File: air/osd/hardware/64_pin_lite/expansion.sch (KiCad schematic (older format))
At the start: 6 parts, among them P11 CONN_1, P2 CONN_20, P3 CONN_20

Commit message: removed vin+ for bat and added pin. Looks nearly done now
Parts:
- added P13: CONN_1, symbol CONN_1
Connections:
- net VIN+: no longer R30.1
- new net: P13.1, R30.1
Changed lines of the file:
@@
-EESchema Schematic File Version 2  date Sun 08 Mar 2015 12:24:24 GMT
+EESchema Schematic File Version 2  date Mon 09 Mar 2015 16:29:56 GMT
 LIBS:lm358
 LIBS:conn_6
@@
 Sheet 5 8
 Title ""
-Date "8 mar 2015"
+Date "9 mar 2015"
 Rev ""
 Comp ""
@@
 Comment4 ""
 $EndDescr
+$Comp
+L CONN_1 P13
+U 1 1 54FDC7F4
+P 5600 2900
+F 0 "P13" H 5680 2900 40  0000 L CNN
+F 1 "CONN_1" H 5600 2955 30  0001 C CNN
+	1    5600 2900
+	1    0    0    -1
+$EndComp
 Wire Wire Line
 	6600 3400 6500 3400
@@
 	6500 4400 6600 4400
 Wire Wire Line
-	5100 2850 5300 2850
-Wire Wire Line
-	5300 2850 5300 3050
+	5450 2900 5300 2900
+Wire Wire Line
+	5300 2900 5300 3050
 Wire Wire Line
 	5300 3650 5550 3650
@@
 	1    0    0    -1
 $EndComp
-Text HLabel 5100 2850 0    45   Input ~ 0
-VIN+
 Text HLabel 5200 4300 0    45   BiDi ~ 0
 MCU_GND

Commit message: hopefully finished
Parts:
- removed C39: 10uF, symbol C
- removed P13: CONN_1, symbol CONN_1
- removed R30: 110K, symbol R
- removed R31: 15K, symbol R
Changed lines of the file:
@@
-EESchema Schematic File Version 2  date Wed 11 Mar 2015 10:11:51 GMT
+EESchema Schematic File Version 2  date Wed 11 Mar 2015 17:51:25 GMT
 LIBS:lm358
 LIBS:conn_6
@@
 Comment4 ""
 $EndDescr
-$Comp
-L CONN_1 P13
-U 1 1 54FDC7F4
-P 5600 2900
-F 0 "P13" H 5680 2900 40  0000 L CNN
-F 1 "CONN_1" H 5600 2955 30  0001 C CNN
-	1    5600 2900
-	1    0    0    -1
-$EndComp
+Text HLabel 4200 3000 2    45   BiDi ~ 0
+XP_PB1
 Wire Wire Line
 	6600 3400 6500 3400
@@
 Wire Wire Line
 	6600 1750 6600 1800
-Connection ~ 5300 4300
-Wire Wire Line
-	5550 4200 5550 4300
-Wire Wire Line
-	5550 4300 5200 4300
-Wire Wire Line
-	5300 4200 5300 4300
-Wire Wire Line
-	5300 3550 5300 3700
 Wire Wire Line
 	6500 4300 6600 4300
@@
 	4100 3200 4200 3200
 Wire Wire Line
-	4750 3000 4100 3000
+	4200 3000 4100 3000
 Connection ~ 6200 2500
 Wire Wire Line
@@
 Wire Wire Line
 	6500 4400 6600 4400
-Wire Wire Line
-	5450 2900 5300 2900
-Wire Wire Line
-	5300 2900 5300 3050
-Wire Wire Line
-	5300 3650 5550 3650
-Wire Wire Line
-	5550 3650 5550 3800
-Connection ~ 5300 3650
-Wire Wire Line
-	5300 3600 4650 3600
-Connection ~ 5300 3600
-Wire Wire Line
-	4650 3600 4650 3000
-Connection ~ 4650 3000
 Wire Wire Line
 	4100 3400 4200 3400
@@
 Text Notes 5500 3350 0    45   ~ 0
 3V max. \nWith values \nshown works \nfrom 2S to 6S\n
-$Comp
-L C C39
-U 1 1 547ED333
-P 5550 4000
-F 0 "C39" H 5600 4100 50  0000 L CNN
-F 1 "10uF" H 5600 3900 50  0000 L CNN
-	1    5550 4000
-	1    0    0    -1
-$EndComp
-Text HLabel 5200 4300 0    45   BiDi ~ 0
-MCU_GND
-$Comp
-L R R31
-U 1 1 547ED2AB
-P 5300 3950
-F 0 "R31" V 5380 3950 50  0000 C CNN
-F 1 "15K" V 5300 3950 50  0000 C CNN
-	1    5300 3950
-	1    0    0    -1
-$EndComp
-$Comp
-L R R30
-U 1 1 547ED2A5
-P 5300 3300
-F 0 "R30" V 5380 3300 50  0000 C CNN
-F 1 "110K" V 5300 3300 50  0000 C CNN
-	1    5300 3300
-	1    0    0    -1
-$EndComp
 Text HLabel 6500 4400 0    45   BiDi ~ 0
 XP_GND
@@
 XP_GND
 $Comp
-L PWR_FLAG #FLG3
+L PWR_FLAG #FLG03
 U 1 1 5474845E
 P 5550 2550
-F 0 "#FLG3" H 5550 2820 30  0001 C CNN
+F 0 "#FLG03" H 5550 2820 30  0001 C CNN
 F 1 "PWR_FLAG" H 5550 2780 30  0000 C CNN
 	1    5550 2550
@@
 $EndComp
 $Comp
-L PWR_FLAG #FLG4
+L PWR_FLAG #FLG04
 U 1 1 54748449
 P 6200 2350
-F 0 "#FLG4" H 6200 2620 30  0001 C CNN
+F 0 "#FLG04" H 6200 2620 30  0001 C CNN
 F 1 "PWR_FLAG" H 6200 2580 30  0000 C CNN
 	1    6200 2350
@@
 Text HLabel 4200 4400 2    45   BiDi ~ 0
 XP_GND
-Text HLabel 4750 3000 2    45   BiDi ~ 0
-XP_PB1
 $EndSCHEMATC

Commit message: after sending V2 board to OSHPark, v2.1
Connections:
- net XP_+3V: now also P2.16 (P16); no longer P2.15 (P15)
- net XP_GND: now also P2.12 (P12), P2.18 (P18), P2.2 (P2), P2.5 (P5), P2.8 (P8), P3.14 (P14); no longer P2.17 (P17), P2.20 (P20), P2.3 (P3), P2.4 (P4), P3.10 (P10)
- net XP_NRST: now also P2.20 (P20); no longer P2.19 (P19)
- net XP_PA0: now also P3.13 (P13); no longer P3.14 (P14)
- net XP_PA1: now also P3.12 (P12); no longer P3.13 (P13)
- net XP_PA11: now also P2.14 (P14); no longer P2.13 (P13)
- net XP_PA12: now also P2.15 (P15); no longer P2.14 (P14)
- net XP_PA13: now also P2.19 (P19); no longer P2.18 (P18)
- net XP_PA14: now also P2.17 (P17); no longer P2.16 (P16)
- net XP_PB6: now also P2.7 (P7); no longer P2.8 (P8)
- net XP_PB7: now also P2.6 (P6); no longer P2.7 (P7)
- net XP_PB8: now also P2.4 (P4); no longer P2.6 (P6)
- net XP_PB9: now also P2.3 (P3); no longer P2.5 (P5)
- net XP_PC0: now also P3.10 (P10); no longer P3.11 (P11)
- net XP_PC1: now also P3.11 (P11); no longer P3.12 (P12)
- net XP_PC12: now also P2.13 (P13); no longer P2.12 (P12)
- no-connect marks 1 -> 0
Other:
- note removed: "3V max. \nWith values \nshown works \nfrom 2S to 6S\n"
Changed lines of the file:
@@
-EESchema Schematic File Version 2  date Wed 11 Mar 2015 17:51:25 GMT
+EESchema Schematic File Version 2  date Thu 12 Mar 2015 15:44:15 GMT
 LIBS:lm358
 LIBS:conn_6
@@
 Sheet 5 8
 Title ""
-Date "11 mar 2015"
+Date "12 mar 2015"
 Rev ""
 Comp ""
@@
 Comment4 ""
 $EndDescr
+Wire Wire Line
+	6600 2700 6500 2700
+Wire Wire Line
+	6600 3400 6500 3400
+Wire Wire Line
+	6600 3200 6500 3200
+Wire Wire Line
+	6600 3000 6500 3000
+Wire Wire Line
+	6500 1750 6600 1750
+Wire Wire Line
+	6600 1750 6600 1800
+Wire Wire Line
+	6500 4300 6600 4300
+Wire Wire Line
+	6500 4100 6600 4100
+Wire Wire Line
+	6500 3900 6600 3900
+Wire Wire Line
+	6500 3700 6600 3700
+Wire Wire Line
+	6500 3500 6600 3500
+Wire Wire Line
+	6500 2900 6600 2900
+Wire Wire Line
+	4100 4400 4200 4400
+Wire Wire Line
+	4100 4200 4200 4200
+Wire Wire Line
+	4100 4000 4200 4000
+Wire Wire Line
+	4100 3800 4200 3800
+Wire Wire Line
+	4100 3600 4200 3600
+Wire Wire Line
+	4100 3200 4200 3200
+Wire Wire Line
+	4200 3000 4100 3000
+Connection ~ 6200 2500
+Wire Wire Line
+	6200 2350 6200 2500
+Wire Wire Line
+	4100 2700 4200 2700
+Wire Wire Line
+	4100 2500 4200 2500
+Wire Wire Line
+	4100 2900 4200 2900
+Wire Wire Line
+	5950 2500 6600 2500
+Wire Wire Line
+	4100 2600 4200 2600
+Wire Wire Line
+	4100 2800 4200 2800
+Wire Wire Line
+	5550 2700 5550 2550
+Connection ~ 5550 2700
+Wire Wire Line
+	4100 3100 4200 3100
+Wire Wire Line
+	4100 3300 4200 3300
+Wire Wire Line
+	4100 3500 4200 3500
+Wire Wire Line
+	4100 3700 4200 3700
+Wire Wire Line
+	4100 3900 4200 3900
+Wire Wire Line
+	4100 4100 4200 4100
+Wire Wire Line
+	4100 4300 4200 4300
+Wire Wire Line
+	6500 2800 6600 2800
+Wire Wire Line
+	6500 3600 6600 3600
+Wire Wire Line
+	6500 3800 6600 3800
+Wire Wire Line
+	6500 4000 6600 4000
+Wire Wire Line
+	6500 4200 6600 4200
+Wire Wire Line
+	6500 4400 6600 4400
+Wire Wire Line
+	4100 3400 4200 3400
+Wire Wire Line
+	6600 3100 6500 3100
+Wire Wire Line
+	6600 3300 6500 3300
+Wire Wire Line
+	6600 2600 5650 2600
+Wire Wire Line
+	5650 2600 5650 2700
+Wire Wire Line
+	5650 2700 5400 2700
+Text HLabel 6500 2900 0    45   BiDi ~ 0
+XP_GND
 Text HLabel 4200 3000 2    45   BiDi ~ 0
 XP_PB1
-Wire Wire Line
-	6600 3400 6500 3400
-Wire Wire Line
-	6600 3200 6500 3200
-Wire Wire Line
-	6600 3000 6500 3000
-Wire Wire Line
-	6500 1750 6600 1750
-Wire Wire Line
-	6600 1750 6600 1800
-Wire Wire Line
-	6500 4300 6600 4300
-Wire Wire Line
-	6500 4100 6600 4100
-Wire Wire Line
-	6500 3900 6600 3900
-Wire Wire Line
-	6500 3700 6600 3700
-Wire Wire Line
-	6500 3500 6600 3500
-Wire Wire Line
-	6500 2900 6600 2900
-Wire Wire Line
-	4100 4400 4200 4400
-Wire Wire Line
-	4100 4200 4200 4200
-Wire Wire Line
-	4100 4000 4200 4000
-Wire Wire Line
-	4100 3800 4200 3800
-Wire Wire Line
-	4100 3600 4200 3600
-Wire Wire Line
-	4100 3200 4200 3200
-Wire Wire Line
-	4200 3000 4100 3000
-Connection ~ 6200 2500
-Wire Wire Line
-	6200 2350 6200 2500
-Wire Wire Line
-	4100 2700 4200 2700
-Wire Wire Line
-	4100 2500 4200 2500
-Wire Wire Line
-	4100 2900 4200 2900
-Wire Wire Line
-	5400 2700 6600 2700
-Wire Wire Line
-	6600 2500 5950 2500
-Wire Wire Line
-	4100 2600 4200 2600
-Wire Wire Line
-	4100 2800 4200 2800
-Wire Wire Line
-	5550 2550 5550 2700
-Connection ~ 5550 2700
-Wire Wire Line
-	4100 3100 4200 3100
-Wire Wire Line
-	4100 3300 4200 3300
-Wire Wire Line
-	4100 3500 4200 3500
-Wire Wire Line
-	4100 3700 4200 3700
-Wire Wire Line
-	4100 3900 4200 3900
-Wire Wire Line
-	4100 4100 4200 4100
-Wire Wire Line
-	4100 4300 4200 4300
-Wire Wire Line
-	6500 2800 6600 2800
-Wire Wire Line
-	6500 3600 6600 3600
-Wire Wire Line
-	6500 3800 6600 3800
-Wire Wire Line
-	6500 4000 6600 4000
-Wire Wire Line
-	6500 4200 6600 4200
-Wire Wire Line
-	6500 4400 6600 4400
-Wire Wire Line
-	4100 3400 4200 3400
-Wire Wire Line
-	6600 3100 6500 3100
-Wire Wire Line
-	6600 3300 6500 3300
-Text HLabel 6500 3000 0    45   BiDi ~ 0
+Text HLabel 6500 2800 0    45   BiDi ~ 0
 XP_PB8
-Text HLabel 4200 3400 2    45   BiDi ~ 0
-XP_GND
-NoConn ~ 6600 2600
+Text HLabel 4200 3800 2    45   BiDi ~ 0
+XP_GND
 Text HLabel 6500 1750 0    45   Output ~ 0
 VIN-
@@
 	0    1    1    0
 $EndComp
-Text Notes 5500 3350 0    45   ~ 0
-3V max. \nWith values \nshown works \nfrom 2S to 6S\n
-Text HLabel 6500 4400 0    45   BiDi ~ 0
-XP_GND
-Text HLabel 6500 2800 0    45   Output ~ 0
+Text HLabel 6500 3600 0    45   BiDi ~ 0
+XP_GND
+Text HLabel 6500 3200 0    45   Output ~ 0
 XP_GND
 $Comp
@@
 	1    0    0    -1
 $EndComp
-Text HLabel 6500 4200 0    45   BiDi ~ 0
+Text HLabel 6500 4300 0    45   BiDi ~ 0
 XP_PA13
 Text HLabel 4200 2800 2    45   Output ~ 0
@@
 Text HLabel 4200 3200 2    45   Input ~ 0
 XP_PC15
-Text HLabel 6500 4300 0    45   Output ~ 0
+Text HLabel 6500 4400 0    45   Output ~ 0
 XP_NRST
 Text HLabel 1900 5450 0    45   BiDi ~ 0
 XP_GND
+Text HLabel 6500 4200 0    45   BiDi ~ 0
+XP_GND
 Text HLabel 6500 4100 0    45   BiDi ~ 0
-XP_GND
-Text HLabel 6500 4000 0    45   BiDi ~ 0
 XP_PA14
+Text HLabel 6500 3900 0    45   BiDi ~ 0
+XP_PA12
 Text HLabel 6500 3800 0    45   BiDi ~ 0
-XP_PA12
+XP_PA11
 Text HLabel 6500 3700 0    45   BiDi ~ 0
-XP_PA11
-Text HLabel 6500 3600 0    45   BiDi ~ 0
 XP_PC12
 Text HLabel 6500 3500 0    45   BiDi ~ 0
@@
 Text HLabel 6500 3300 0    45   BiDi ~ 0
 XP_PB5
-Text HLabel 6500 3900 0    45   BiDi ~ 0
+Text HLabel 6500 4000 0    45   BiDi ~ 0
 XP_+3V
-Text HLabel 6500 3200 0    45   BiDi ~ 0
+Text HLabel 6500 3100 0    45   BiDi ~ 0
 XP_PB6
-Text HLabel 6500 3100 0    45   BiDi ~ 0
+Text HLabel 6500 3000 0    45   BiDi ~ 0
 XP_PB7
-Text HLabel 6500 2900 0    45   BiDi ~ 0
+Text HLabel 6500 2700 0    45   BiDi ~ 0
 XP_PB9
 Text HLabel 4200 4300 2    45   BiDi ~ 0
@@
 Text HLabel 4200 3900 2    45   BiDi ~ 0
 XP_PC3
-Text HLabel 4200 3800 2    45   BiDi ~ 0
+Text HLabel 4200 3700 2    45   BiDi ~ 0
 XP_PA0
-Text HLabel 4200 3700 2    45   BiDi ~ 0
+Text HLabel 4200 3600 2    45   BiDi ~ 0
 XP_PA1
-Text HLabel 4200 3600 2    45   BiDi ~ 0
+Text HLabel 4200 3500 2    45   BiDi ~ 0
 XP_PC1
-Text HLabel 4200 3500 2    45   BiDi ~ 0
+Text HLabel 4200 3400 2    45   BiDi ~ 0
 XP_PC0
 Text HLabel 4200 3300 2    45   BiDi ~ 0

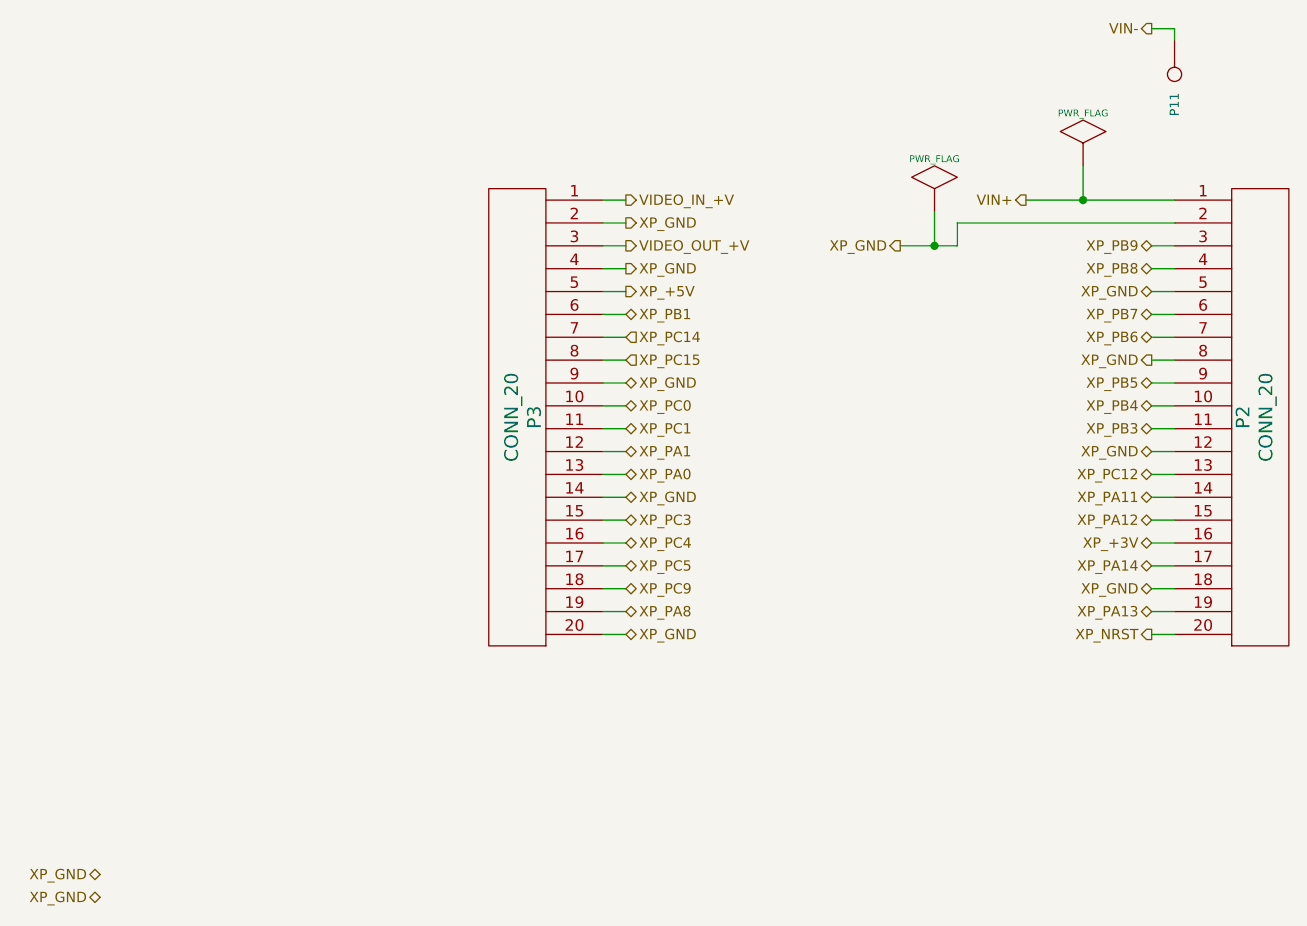
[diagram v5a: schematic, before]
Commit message: added some 3 terminal EMI filters to the board
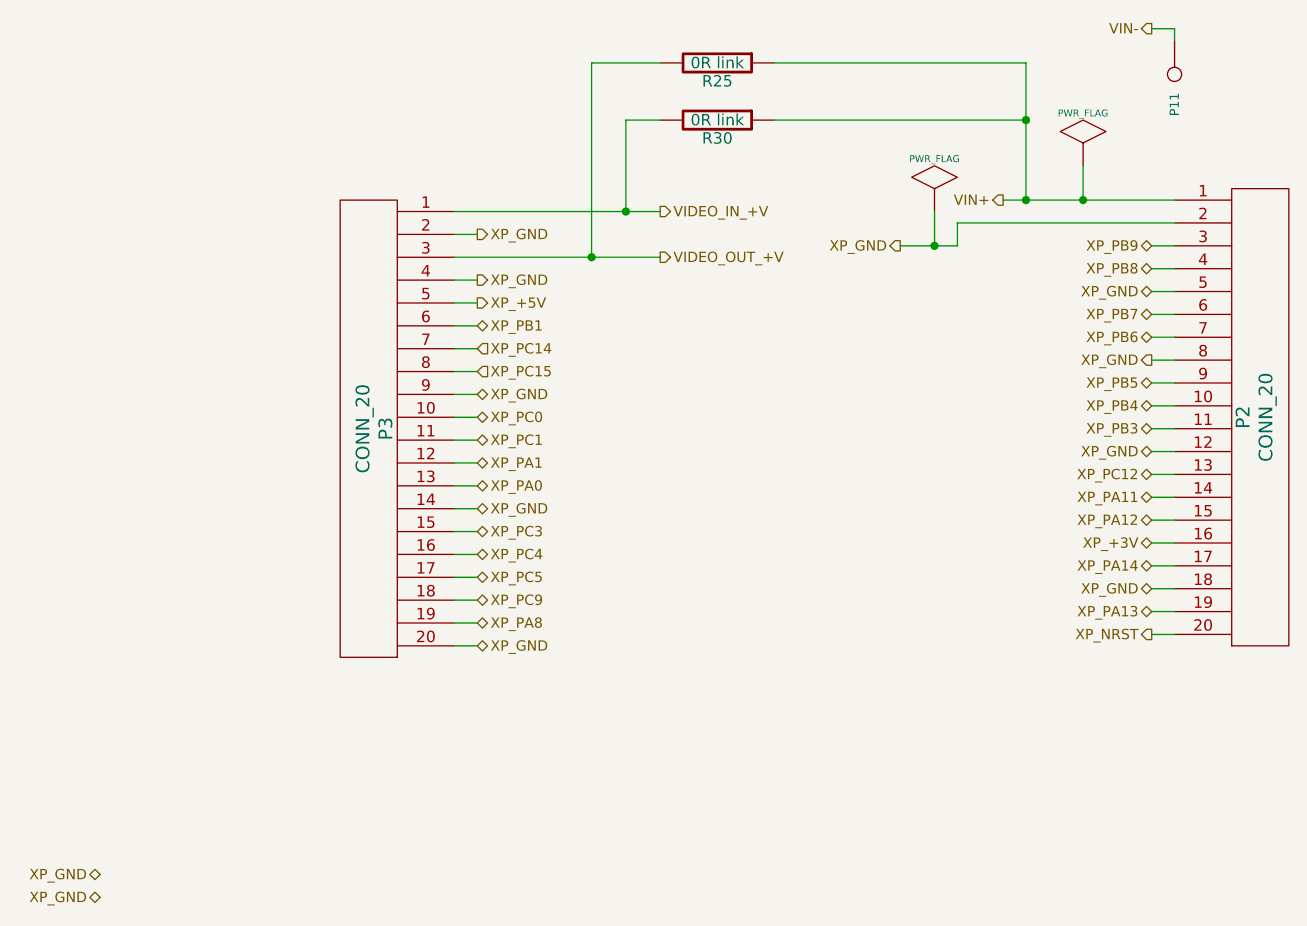
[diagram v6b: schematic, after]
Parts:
- added R25, R30: 0R link, symbol R
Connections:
- net VIDEO_IN_+V: now also R30.2
- net VIDEO_OUT_+V: now also R25.2
- net VIN+: now also R25.1, R30.1
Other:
- moved on the sheet: P3
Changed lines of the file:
@@
-EESchema Schematic File Version 2  date Thu 12 Mar 2015 15:44:15 GMT
+EESchema Schematic File Version 2  date Wed 17 Jun 2015 00:34:32 BST
 LIBS:lm358
 LIBS:conn_6
@@
 LIBS:74lvc1g86
 LIBS:R0link
+LIBS:emi_filter
 LIBS:osd-cache
 EELAYER 25  0
@@
 Sheet 5 8
 Title ""
-Date "12 mar 2015"
+Date "16 jun 2015"
 Rev ""
 Comp ""
@@
 Comment4 ""
 $EndDescr
+Connection ~ 4050 2750
+Wire Wire Line
+	4350 1900 4050 1900
+Wire Wire Line
+	4050 1900 4050 2750
+Connection ~ 5950 2150
+Wire Wire Line
+	4850 2150 5950 2150
 Wire Wire Line
 	6600 2700 6500 2700
@@
 	6500 2900 6600 2900
 Wire Wire Line
-	4100 4400 4200 4400
-Wire Wire Line
-	4100 4200 4200 4200
-Wire Wire Line
-	4100 4000 4200 4000
-Wire Wire Line
-	4100 3800 4200 3800
-Wire Wire Line
-	4100 3600 4200 3600
-Wire Wire Line
-	4100 3200 4200 3200
-Wire Wire Line
-	4200 3000 4100 3000
+	3450 4450 3550 4450
+Wire Wire Line
+	3450 4250 3550 4250
+Wire Wire Line
+	3450 4050 3550 4050
+Wire Wire Line
+	3450 3850 3550 3850
+Wire Wire Line
+	3450 3650 3550 3650
+Wire Wire Line
+	3450 3250 3550 3250
+Wire Wire Line
+	3550 3050 3450 3050
 Connection ~ 6200 2500
 Wire Wire Line
 	6200 2350 6200 2500
 Wire Wire Line
-	4100 2700 4200 2700
-Wire Wire Line
-	4100 2500 4200 2500
-Wire Wire Line
-	4100 2900 4200 2900
-Wire Wire Line
-	5950 2500 6600 2500
-Wire Wire Line
-	4100 2600 4200 2600
-Wire Wire Line
-	4100 2800 4200 2800
+	3450 2750 4350 2750
+Wire Wire Line
+	3450 2550 4350 2550
+Wire Wire Line
+	3450 2950 3550 2950
+Wire Wire Line
+	6600 2500 5850 2500
+Wire Wire Line
+	3450 2650 3550 2650
+Wire Wire Line
+	3450 2850 3550 2850
 Wire Wire Line
 	5550 2700 5550 2550
 Connection ~ 5550 2700
 Wire Wire Line
-	4100 3100 4200 3100
-Wire Wire Line
-	4100 3300 4200 3300
-Wire Wire Line
-	4100 3500 4200 3500
-Wire Wire Line
-	4100 3700 4200 3700
-Wire Wire Line
-	4100 3900 4200 3900
-Wire Wire Line
-	4100 4100 4200 4100
-Wire Wire Line
-	4100 4300 4200 4300
+	3450 3150 3550 3150
+Wire Wire Line
+	3450 3350 3550 3350
+Wire Wire Line
+	3450 3550 3550 3550
+Wire Wire Line
+	3450 3750 3550 3750
+Wire Wire Line
+	3450 3950 3550 3950
+Wire Wire Line
+	3450 4150 3550 4150
+Wire Wire Line
+	3450 4350 3550 4350
 Wire Wire Line
 	6500 2800 6600 2800
@@
 	6500 4400 6600 4400
 Wire Wire Line
-	4100 3400 4200 3400
+	3450 3450 3550 3450
 Wire Wire Line
 	6600 3100 6500 3100
@@
 Wire Wire Line
 	5650 2700 5400 2700
+Wire Wire Line
+	4850 1900 5950 1900
+Wire Wire Line
+	5950 1900 5950 2500
+Connection ~ 5950 2500
+Wire Wire Line
+	4350 2150 4200 2150
+Wire Wire Line
+	4200 2150 4200 2550
+Connection ~ 4200 2550
+$Comp
+L R R30
+U 1 1 5580AC4E
+P 4600 2150
+F 0 "R30" V 4680 2150 50  0000 C CNN
+F 1 "0R link" V 4600 2150 50  0000 C CNN
+	1    4600 2150
+	0    1    1    0
+$EndComp
+$Comp
+L R R25
+U 1 1 5580AC49
+P 4600 1900
+F 0 "R25" V 4680 1900 50  0000 C CNN
+F 1 "0R link" V 4600 1900 50  0000 C CNN
+	1    4600 1900
+	0    1    1    0
+$EndComp
 Text HLabel 6500 2900 0    45   BiDi ~ 0
 XP_GND
-Text HLabel 4200 3000 2    45   BiDi ~ 0
+Text HLabel 3550 3050 2    45   BiDi ~ 0
 XP_PB1
 Text HLabel 6500 2800 0    45   BiDi ~ 0
 XP_PB8
-Text HLabel 4200 3800 2    45   BiDi ~ 0
+Text HLabel 3550 3850 2    45   BiDi ~ 0
 XP_GND
 Text HLabel 6500 1750 0    45   Output ~ 0
@@
 Text HLabel 6500 4300 0    45   BiDi ~ 0
 XP_PA13
-Text HLabel 4200 2800 2    45   Output ~ 0
-XP_GND
-Text HLabel 4200 2600 2    45   Output ~ 0
-XP_GND
-Text HLabel 4200 2700 2    45   Output ~ 0
+Text HLabel 3550 2850 2    45   Output ~ 0
+XP_GND
+Text HLabel 3550 2650 2    45   Output ~ 0
+XP_GND
+Text HLabel 4350 2750 2    45   Output ~ 0
 VIDEO_OUT_+V
-Text HLabel 4200 2500 2    45   Output ~ 0
+Text HLabel 4350 2550 2    45   Output ~ 0
 VIDEO_IN_+V
 Text HLabel 5400 2700 0    45   Output ~ 0
 XP_GND
-Text HLabel 4200 2900 2    45   Output ~ 0
+Text HLabel 3550 2950 2    45   Output ~ 0
 XP_+5V
 $Comp
 L CONN_20 P3
 U 1 1 54746DE4
-P 3750 3450
-F 0 "P3" V 3700 3450 60  0000 C CNN
-F 1 "CONN_20" V 3800 3450 60  0000 C CNN
-	1    3750 3450
+P 3100 3500
+F 0 "P3" V 3050 3500 60  0000 C CNN
+F 1 "CONN_20" V 3150 3500 60  0000 C CNN
+	1    3100 3500
 	-1   0    0    -1
 $EndComp
@@
 Text HLabel 1900 5550 0    45   BiDi ~ 0
 XP_GND
-Text HLabel 5950 2500 0    45   Output ~ 0
+Text HLabel 5850 2500 0    45   Output ~ 0
 VIN+
-Text HLabel 4200 3200 2    45   Input ~ 0
+Text HLabel 3550 3250 2    45   Input ~ 0
 XP_PC15
 Text HLabel 6500 4400 0    45   Output ~ 0
@@
 Text HLabel 6500 2700 0    45   BiDi ~ 0
 XP_PB9
-Text HLabel 4200 4300 2    45   BiDi ~ 0
+Text HLabel 3550 4350 2    45   BiDi ~ 0
 XP_PA8
-Text HLabel 4200 4200 2    45   BiDi ~ 0
+Text HLabel 3550 4250 2    45   BiDi ~ 0
 XP_PC9
-Text HLabel 4200 4100 2    45   BiDi ~ 0
+Text HLabel 3550 4150 2    45   BiDi ~ 0
 XP_PC5
-Text HLabel 4200 4000 2    45   BiDi ~ 0
+Text HLabel 3550 4050 2    45   BiDi ~ 0
 XP_PC4
-Text HLabel 4200 3900 2    45   BiDi ~ 0
+Text HLabel 3550 3950 2    45   BiDi ~ 0
 XP_PC3
-Text HLabel 4200 3700 2    45   BiDi ~ 0
+Text HLabel 3550 3750 2    45   BiDi ~ 0
 XP_PA0
-Text HLabel 4200 3600 2    45   BiDi ~ 0
+Text HLabel 3550 3650 2    45   BiDi ~ 0
 XP_PA1
-Text HLabel 4200 3500 2    45   BiDi ~ 0
+Text HLabel 3550 3550 2    45   BiDi ~ 0
 XP_PC1
-Text HLabel 4200 3400 2    45   BiDi ~ 0
+Text HLabel 3550 3450 2    45   BiDi ~ 0
 XP_PC0
-Text HLabel 4200 3300 2    45   BiDi ~ 0
-XP_GND
-Text HLabel 4200 3100 2    45   Input ~ 0
+Text HLabel 3550 3350 2    45   BiDi ~ 0
+XP_GND
+Text HLabel 3550 3150 2    45   Input ~ 0
 XP_PC14
-Text HLabel 4200 4400 2    45   BiDi ~ 0
+Text HLabel 3550 4450 2    45   BiDi ~ 0
 XP_GND
 $EndSCHEMATC
